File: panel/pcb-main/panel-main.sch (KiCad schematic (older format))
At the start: 14 parts

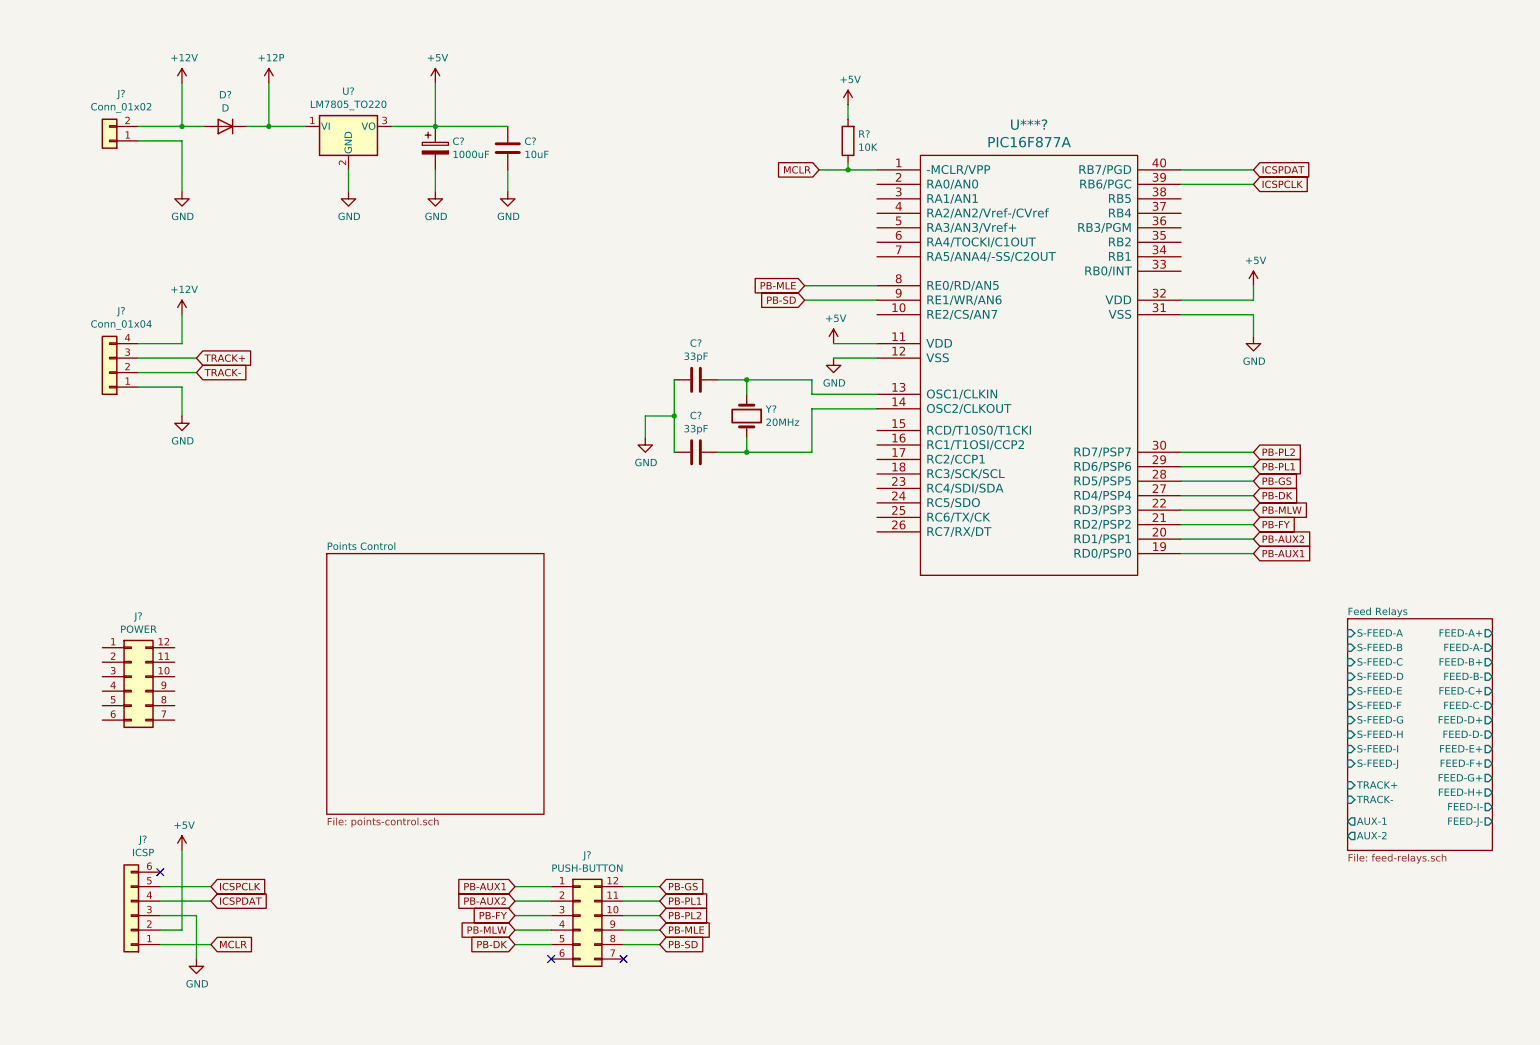
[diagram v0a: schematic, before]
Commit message: PCB Updates and added panel-fw project.
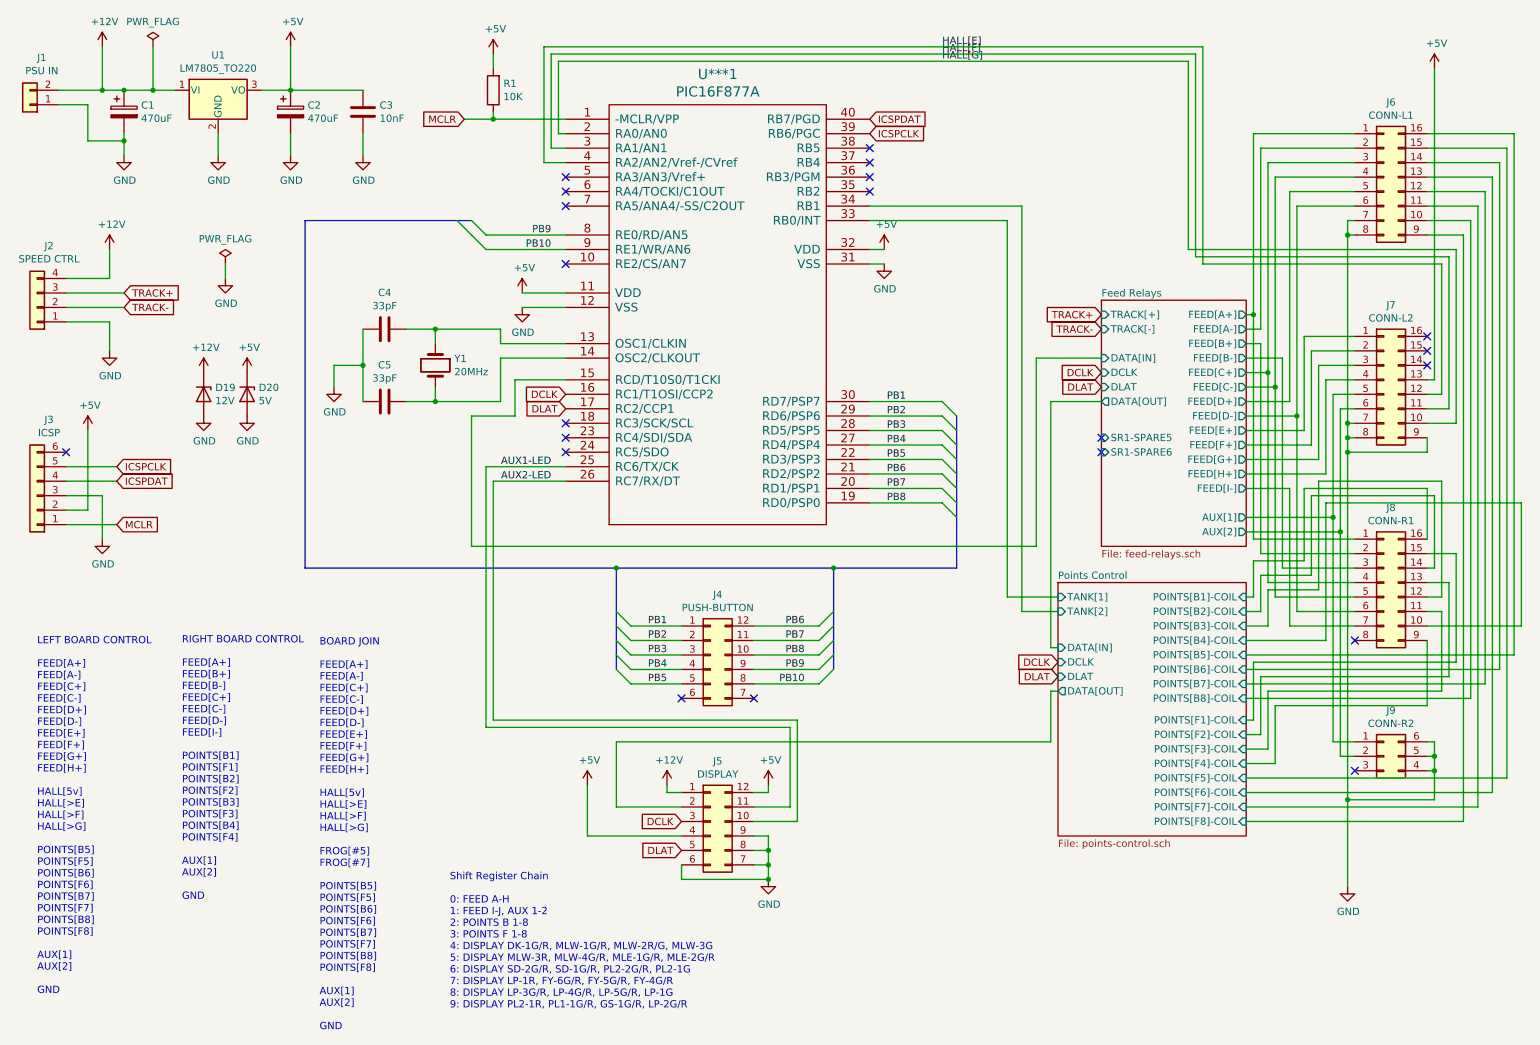
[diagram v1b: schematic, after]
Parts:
- removed D?: D, symbol Device:D
- added C1: 470uF, Capacitors_THT:CP_Radial_D10.0mm_P5.00mm, symbol Device:CP
- added D19: 12V, Diodes_THT:D_DO-15_P10.16mm_Horizontal, symbol Device:D_Zener
- added D20: 5V, Diodes_THT:D_DO-15_P10.16mm_Horizontal, symbol Device:D_Zener
- added J6: CONN-L1, carnivalben:Wire_Pads_Edge_2x8, symbol Connector_Generic:Conn_02x08_Counter_Clockwise
- added J7: CONN-L2, carnivalben:Wire_Pads_Edge_2x8, symbol Connector_Generic:Conn_02x08_Counter_Clockwise
- added J8: CONN-R1, carnivalben:Wire_Pads_Edge_2x8, symbol Connector_Generic:Conn_02x08_Counter_Clockwise
- added J9: CONN-R2, carnivalben:Wire_Pads_Edge_2x3, symbol Connector_Generic:Conn_02x03_Counter_Clockwise
- C2: renamed from C?; value 1000uF -> 470uF; footprint (none) -> Capacitors_THT:CP_Radial_D10.0mm_P5.00mm
- C3: renamed from C?; value 10uF -> 10nF; footprint (none) -> Capacitors_THT:C_Disc_D4.7mm_W2.5mm_P5.00mm
- C4, C5: renamed from C?; footprint (none) -> Capacitors_THT:C_Disc_D3.4mm_W2.1mm_P2.50mm
- J1: renamed from J?; value Conn_01x02 -> PSU IN; footprint (none) -> carnivalben:Wire_Pads_Edge_1x2
- J2: renamed from J?; value Conn_01x04 -> SPEED CTRL; footprint (none) -> carnivalben:DIN_Socket_Edge_Solder_4pin
- J3: renamed from J?; footprint (none) -> Pin_Headers:Pin_Header_Straight_1x06_Pitch2.54mm
- J4: renamed from J?; footprint (none) -> Pin_Headers:Pin_Header_Straight_2x06_Pitch2.54mm
- J5: renamed from J?; value POWER -> DISPLAY; footprint (none) -> Pin_Headers:Pin_Header_Straight_2x06_Pitch2.54mm
- R1: renamed from R?; footprint (none) -> Resistors_THT:R_Axial_DIN0207_L6.3mm_D2.5mm_P10.16mm_Horizontal
- U***1: renamed from U***?; footprint (none) -> Housings_DIP:DIP-40_W15.24mm_LongPads
- U1: renamed from U?; footprint Package_TO_SOT_THT:TO-220-3_Vertical -> TO_SOT_Packages_THT:TO-220-3_Vertical
- Y1: renamed from Y?; footprint (none) -> Crystals:Crystal_HC49-U_Vertical
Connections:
- net +12P is gone; now on net +12V: U1.1 (VI)
- net +12V: now also J5.1 (Pin_1), C1.1, D19.1 (K)
- net +5V: now also J5.12 (Pin_12), J5.4 (Pin_4), D20.1 (K), J7.13 (Pin_13)
- net GND: now also J5.6 (Pin_6), J5.7 (Pin_7), J5.8 (Pin_8), J5.9 (Pin_9), C1.2, D19.2 (A), D20.2 (A), J6.7 (Pin_7), J6.8 (Pin_8), J7.7 (Pin_7), J7.8 (Pin_8), J7.9 (Pin_9), J9.4 (Pin_4), J9.5 (Pin_5), J9.6 (Pin_6)
- net AUX2-LED: now reaches J5.10 (Pin_10)
- net AUX2-LED: now also U***1.26 (RC7/RX/DT)
- net AUX1-LED: now reaches J5.11 (Pin_11)
- net AUX1-LED: now also U***1.25 (RC6/TX/CK)
- net Points Control/DATA[OUT]: now reaches J5.2 (Pin_2)
- net DCLK: now reaches J5.3 (Pin_3)
- net DCLK: now also U***1.16 (RC1/T1OSI/CCP2)
- net DLAT: now reaches J5.5 (Pin_5)
- net DLAT: now also U***1.17 (RC2/CCP1)
- net Feed Relays/DATA[IN]: now reaches U***1.15 (RCD/T10S0/T1CKI)
- net HALL[G]: now reaches U***1.2 (RA0/AN0)
- net HALL[G]: now also J7.10 (Pin_10)
- net HALL[F]: now reaches U***1.3 (RA1/AN1)
- net HALL[F]: now also J7.11 (Pin_11)
- net Points Control/TANK[1]: now reaches U***1.33 (RB0/INT)
- net Points Control/TANK[2]: now reaches U***1.34 (RB1)
- net HALL[E]: now reaches U***1.4 (RA2/AN2/Vref-/CVref)
- net HALL[E]: now also J7.12 (Pin_12)
- net PB-AUX1 renamed PB1
- net PB1: now also U***1.30 (RD7/PSP7); no longer U***1.19 (RD0/PSP0)
- net PB-AUX2 renamed PB2
- net PB2: now also U***1.29 (RD6/PSP6); no longer U***1.20 (RD1/PSP1)
- net PB-DK renamed PB4
- net PB4: now also J4.4 (Pin_4); no longer J4.5 (Pin_5)
- net PB-FY renamed PB3
- net PB3: now also U***1.28 (RD5/PSP5); no longer U***1.21 (RD2/PSP2)
- net PB-GS renamed PB6
- net PB6: now also U***1.21 (RD2/PSP2); no longer U***1.28 (RD5/PSP5)
- net PB-MLE renamed PB9
- net PB-MLW renamed PB5
- net PB5: now also J4.5 (Pin_5); no longer J4.4 (Pin_4)
- net PB-PL1 renamed PB7
- net PB7: now also U***1.20 (RD1/PSP1); no longer U***1.29 (RD6/PSP6)
- net PB-PL2 renamed PB8
- net PB8: now also U***1.19 (RD0/PSP0); no longer U***1.30 (RD7/PSP7)
- net PB-SD renamed PB10
- new net Feed Relays/AUX[1]: J7.5 (Pin_5), J9.1 (Pin_1)
- new net Feed Relays/AUX[2]: J7.6 (Pin_6), J9.2 (Pin_2)
- new net Feed Relays/FEED[A+]: J6.1 (Pin_1), J8.1 (Pin_1)
- new net Feed Relays/FEED[A-]: J6.2 (Pin_2)
- new net Feed Relays/FEED[B+]: J8.2 (Pin_2)
- new net Feed Relays/FEED[B-]: J8.3 (Pin_3)
- new net Feed Relays/FEED[C+]: J6.3 (Pin_3), J8.4 (Pin_4)
- new net Feed Relays/FEED[C-]: J6.4 (Pin_4), J8.5 (Pin_5)
- new net Feed Relays/FEED[D+]: J6.5 (Pin_5)
- new net Feed Relays/FEED[D-]: J6.6 (Pin_6), J8.6 (Pin_6)
- new net Feed Relays/FEED[E+]: J7.1 (Pin_1)
- new net Feed Relays/FEED[F+]: J7.2 (Pin_2)
- new net Feed Relays/FEED[G+]: J7.3 (Pin_3)
- new net Feed Relays/FEED[H+]: J7.4 (Pin_4)
- new net Feed Relays/FEED[I-]: J8.7 (Pin_7)
- new net Points Control/POINTS[B1]-COIL: J8.16 (Pin_16)
- new net Points Control/POINTS[B2]-COIL: J8.14 (Pin_14)
- new net Points Control/POINTS[B3]-COIL: J8.12 (Pin_12)
- new net Points Control/POINTS[B4]-COIL: J8.10 (Pin_10)
- new net Points Control/POINTS[B5]-COIL: J6.16 (Pin_16)
- new net Points Control/POINTS[B6]-COIL: J6.14 (Pin_14)
- new net Points Control/POINTS[B7]-COIL: J6.12 (Pin_12)
- new net Points Control/POINTS[B8]-COIL: J6.10 (Pin_10)
- new net Points Control/POINTS[F1]-COIL: J8.15 (Pin_15)
- new net Points Control/POINTS[F2]-COIL: J8.13 (Pin_13)
- new net Points Control/POINTS[F3]-COIL: J8.11 (Pin_11)
- new net Points Control/POINTS[F4]-COIL: J8.9 (Pin_9)
- new net Points Control/POINTS[F5]-COIL: J6.15 (Pin_15)
- new net Points Control/POINTS[F6]-COIL: J6.13 (Pin_13)
- new net Points Control/POINTS[F7]-COIL: J6.11 (Pin_11)
- new net Points Control/POINTS[F8]-COIL: J6.9 (Pin_9)
- no-connect marks 3 -> 21
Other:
- note added: "BOARD JOIN\n\nFEED[A+]\nFEED[A-]\nFEED[C+]\nFEED[C-]\nFEED[D+]\nFEED[D-]\nFEED[E+]\nFEED[F+]\nFEED[G+]\nFEED[H+]\n\nHALL[5v]\nHALL[>E]\nHALL[>F]\nHALL[>G]\n\nFROG[#5]\nFROG[#7]\n\nPOINTS[B5]\nPOINTS[F5]\nPOINTS[B6]\nPOINTS[F6]\nPOINTS[B7]\nPOINTS[F7]\nPOINTS[B8]\nPOINTS[F8]\n\nAUX[1]\nAUX[2]\n\nGND"
- note added: "LEFT BOARD CONTROL\n\nFEED[A+]\nFEED[A-]\nFEED[C+]\nFEED[C-]\nFEED[D+]\nFEED[D-]\nFEED[E+]\nFEED[F+]\nFEED[G+]\nFEED[H+]\n\nHALL[5v]\nHALL[>E]\nHALL[>F]\nHALL[>G]\n\nPOINTS[B5]\nPOINTS[F5]\nPOINTS[B6]\nPOINTS[F6]\nPOINTS[B7]\nPOINTS[F7]\nPOINTS[B8]\nPOINTS[F8]\n\nAUX[1]\nAUX[2]\n\nGND"
- note added: "RIGHT BOARD CONTROL\n\nFEED[A+]\nFEED[B+]\nFEED[B-]\nFEED[C+]\nFEED[C-]\nFEED[D-]\nFEED[I-]\n\nPOINTS[B1]\nPOINTS[F1]\nPOINTS[B2]\nPOINTS[F2]\nPOINTS[B3]\nPOINTS[F3]\nPOINTS[B4]\nPOINTS[F4]\n\nAUX[1]\nAUX[2]\n\nGND"
- note added: "Shift Register Chain\n\n0: FEED A-H\n1: FEED I-J, AUX 1-2\n2: POINTS B 1-8\n3: POINTS F 1-8\n4: DISPLAY DK-1G/R, MLW-1G/R, MLW-2R/G, MLW-3G\n5: DISPLAY MLW-3R, MLW-4G/R, MLE-1G/R, MLE-2G/R\n6: DISPLAY SD-2G/R, SD-1G/R, PL2-2G/R, PL2-1G\n7: DISPLAY LP-1R, FY-6G/R, FY-5G/R, FY-4G/R\n8: DISPLAY LP-3G/R, LP-4G/R, LP-5G/R, LP-1G\n9: DISPLAY PL2-1R, PL1-1G/R, GS-1G/R, LP-2G/R"
- moved on the sheet: C2, C3, C4, C5, J1, J2, J3, J4, J5, R1, U***1, U1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

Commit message: Main PCB Update - MOSFETS on Points, 3 tanks.
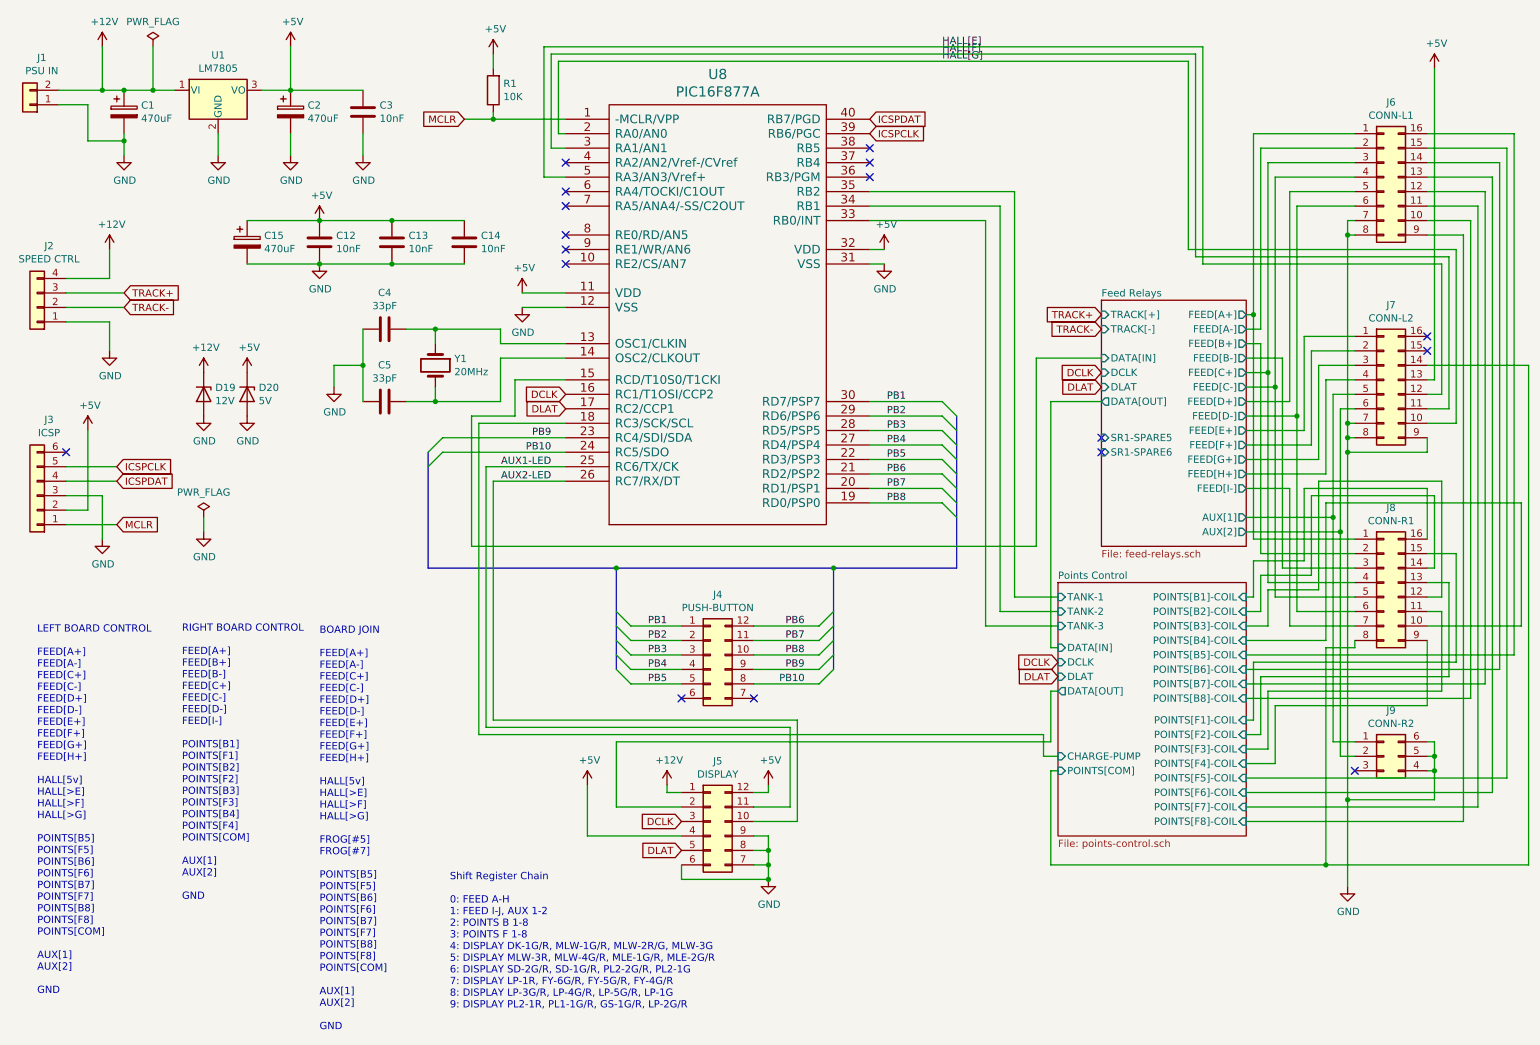
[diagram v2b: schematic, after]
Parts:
- added C12, C13, C14: 10nF, Capacitors_THT:C_Disc_D4.7mm_W2.5mm_P5.00mm, symbol Device:C
- added C15: 470uF, Capacitors_THT:CP_Radial_D10.0mm_P5.00mm, symbol Device:CP
- U1: value LM7805_TO220 -> LM7805; footprint TO_SOT_Packages_THT:TO-220-3_Vertical -> TO_SOT_Packages_THT:TO-220-3_Horizontal
- renumbered U***1 to U8
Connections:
- net +5V: now also C12.1, C13.1, C14.1, C15.1
- net GND: now also C12.2, C13.2, C14.2, C15.2
- net HALL[E]: now also U8.5 (RA3/AN3/Vref+); no longer U8.4 (RA2/AN2/Vref-/CVref)
- net PB10: now also U8.24 (RC5/SDO); no longer U8.9 (RE1/WR/AN6)
- net PB9: now also U8.23 (RC4/SDI/SDA); no longer U8.8 (RE0/RD/AN5)
- net Points Control/CHARGE-PUMP: now reaches U8.18 (RC3/SCK/SCL)
- net Points Control/TANK-1: now reaches U8.35 (RB2)
- net Points Control/POINTS[COM]: now reaches J7.14 (Pin_14)
- net Points Control/POINTS[COM]: now also J8.8 (Pin_8)
- net Points Control/TANK[1] renamed Points Control/TANK-3
- net Points Control/TANK[2] renamed Points Control/TANK-2
- no-connect marks 21 -> 17
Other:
- note added: "BOARD JOIN\n\nFEED[A+]\nFEED[A-]\nFEED[C+]\nFEED[C-]\nFEED[D+]\nFEED[D-]\nFEED[E+]\nFEED[F+]\nFEED[G+]\nFEED[H+]\n\nHALL[5v]\nHALL[>E]\nHALL[>F]\nHALL[>G]\n\nFROG[#5]\nFROG[#7]\n\nPOINTS[B5]\nPOINTS[F5]\nPOINTS[B6]\nPOINTS[F6]\nPOINTS[B7]\nPOINTS[F7]\nPOINTS[B8]\nPOINTS[F8]\nPOINTS[COM]\n\nAUX[1]\nAUX[2]\n\nGND"
- note added: "LEFT BOARD CONTROL\n\nFEED[A+]\nFEED[A-]\nFEED[C+]\nFEED[C-]\nFEED[D+]\nFEED[D-]\nFEED[E+]\nFEED[F+]\nFEED[G+]\nFEED[H+]\n\nHALL[5v]\nHALL[>E]\nHALL[>F]\nHALL[>G]\n\nPOINTS[B5]\nPOINTS[F5]\nPOINTS[B6]\nPOINTS[F6]\nPOINTS[B7]\nPOINTS[F7]\nPOINTS[B8]\nPOINTS[F8]\nPOINTS[COM]\n\nAUX[1]\nAUX[2]\n\nGND"
- note added: "RIGHT BOARD CONTROL\n\nFEED[A+]\nFEED[B+]\nFEED[B-]\nFEED[C+]\nFEED[C-]\nFEED[D-]\nFEED[I-]\n\nPOINTS[B1]\nPOINTS[F1]\nPOINTS[B2]\nPOINTS[F2]\nPOINTS[B3]\nPOINTS[F3]\nPOINTS[B4]\nPOINTS[F4]\nPOINTS[COM]\n\nAUX[1]\nAUX[2]\n\nGND"
- note removed: "BOARD JOIN\n\nFEED[A+]\nFEED[A-]\nFEED[C+]\nFEED[C-]\nFEED[D+]\nFEED[D-]\nFEED[E+]\nFEED[F+]\nFEED[G+]\nFEED[H+]\n\nHALL[5v]\nHALL[>E]\nHALL[>F]\nHALL[>G]\n\nFROG[#5]\nFROG[#7]\n\nPOINTS[B5]\nPOINTS[F5]\nPOINTS[B6]\nPOINTS[F6]\nPOINTS[B7]\nPOINTS[F7]\nPOINTS[B8]\nPOINTS[F8]\n\nAUX[1]\nAUX[2]\n\nGND"
- note removed: "LEFT BOARD CONTROL\n\nFEED[A+]\nFEED[A-]\nFEED[C+]\nFEED[C-]\nFEED[D+]\nFEED[D-]\nFEED[E+]\nFEED[F+]\nFEED[G+]\nFEED[H+]\n\nHALL[5v]\nHALL[>E]\nHALL[>F]\nHALL[>G]\n\nPOINTS[B5]\nPOINTS[F5]\nPOINTS[B6]\nPOINTS[F6]\nPOINTS[B7]\nPOINTS[F7]\nPOINTS[B8]\nPOINTS[F8]\n\nAUX[1]\nAUX[2]\n\nGND"
- note removed: "RIGHT BOARD CONTROL\n\nFEED[A+]\nFEED[B+]\nFEED[B-]\nFEED[C+]\nFEED[C-]\nFEED[D-]\nFEED[I-]\n\nPOINTS[B1]\nPOINTS[F1]\nPOINTS[B2]\nPOINTS[F2]\nPOINTS[B3]\nPOINTS[F3]\nPOINTS[B4]\nPOINTS[F4]\n\nAUX[1]\nAUX[2]\n\nGND"

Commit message: Completed all PCBs and added gerber files
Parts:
- added D5: RUNNING, LEDs:LED_D5.0mm, symbol Device:LED
- added D6: CHARGING, LEDs:LED_D5.0mm, symbol Device:LED
- added D7: SWITCHING, LEDs:LED_D5.0mm, symbol Device:LED
- added J11: REVERSE, Pin_Headers:Pin_Header_Straight_2x03_Pitch2.54mm, symbol Connector_Generic:Conn_02x03_Odd_Even
- added R18: 47K, Resistors_THT:R_Axial_DIN0207_L6.3mm_D2.5mm_P10.16mm_Horizontal, symbol Device:R
- added R19: 10K, Resistors_THT:R_Axial_DIN0207_L6.3mm_D2.5mm_P10.16mm_Horizontal, symbol Device:R
- added R38, R39, R40: 240, Resistors_THT:R_Axial_DIN0207_L6.3mm_D2.5mm_P10.16mm_Horizontal, symbol Device:R
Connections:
- net GND: now also R19.1, R38.1, R39.1, R40.1
- net HALL[E]: now also U8.4 (RA2/AN2/Vref-/CVref); no longer U8.5 (RA3/AN3/Vref+)
- net Points Control/POINTS[COM]: now also R18.2
- net TRACK+: now also J11.4 (Pin_4); no longer J2.3 (Pin_3)
- net TRACK-: now also J11.3 (Pin_3); no longer J2.2 (Pin_2)
- net at U8.36 (RB3/PGM): now also D5.2 (A)
- net at U8.37 (RB4): now also D6.2 (A)
- net at U8.38 (RB5): now also D7.2 (A)
- net Points Control/TANK-1: no longer names the net of U8.35 (RB2)
- net Points Control/TANK-2: no longer names the net of U8.34 (RB1)
- net Points Control/TANK-3: no longer names the net of U8.33 (RB0/INT)
- new net: D7.1 (K), R40.2
- new net: D6.1 (K), R39.2
- new net: D5.1 (K), R38.2
- new net CHG-LVL: R18.1, R19.2, U8.5 (RA3/AN3/Vref+)
- new net TFEED[+]: J11.1 (Pin_1), J11.6 (Pin_6), J2.3 (Pin_3)
- new net TFEED[-]: J11.2 (Pin_2), J11.5 (Pin_5), J2.2 (Pin_2)
- no-connect marks 17 -> 16
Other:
- moved on the sheet: C12, C13, C14, C15, D19, D20
